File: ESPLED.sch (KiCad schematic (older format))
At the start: 44 parts, among them CON1 BARREL_JACK, J1 USB_B_Micro, J2 LED_CON_RGB, J3 LED_CON_WW, J4 MIC, P1 LED_CON_SCREW, P2 LED_CON_SCREW, P3 LED_CON_SCREW, Q1 IRLZ34N, Q2 IRLZ34N, Q3 IRLZ34N, Q4 IRLZ34N, Q5 IRLZ34N, SW1 Reset, SW2 Program, SW3 Mode, U1 AMS1117-3.3, U2 ESP-07v2, U3 INTERFACE-CH340G, U4 DS18B20, Y1 Crystal

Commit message: Ongoin reordering. Will probably
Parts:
- renumbered Q3 to Q1, Q1 to Q3
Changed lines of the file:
@@
 $EndComp
 $Comp
-L Transistor_FET:IRLZ34N Q3
+L Transistor_FET:IRLZ34N Q1
 U 1 1 5967CE85
 P 3200 3450
-F 0 "Q3" H 3400 3500 50  0000 L CNN
+F 0 "Q1" H 3400 3500 50  0000 L CNN
 F 1 "IRLZ34N" H 3400 3400 50  0000 L CNN
 F 2 "Package_TO_SOT_THT:TO-220-3_Horizontal_TabDown" H 3400 3550 50  0001 C CNN
@@
 $EndComp
 $Comp
-L Transistor_FET:IRLZ34N Q1
+L Transistor_FET:IRLZ34N Q3
 U 1 1 5967CF69
 P 1350 3450
-F 0 "Q1" H 1550 3500 50  0000 L CNN
+F 0 "Q3" H 1550 3500 50  0000 L CNN
 F 1 "IRLZ34N" H 1550 3400 50  0000 L CNN
 F 2 "Package_TO_SOT_THT:TO-220-3_Horizontal_TabDown" H 1550 3550 50  0001 C CNN

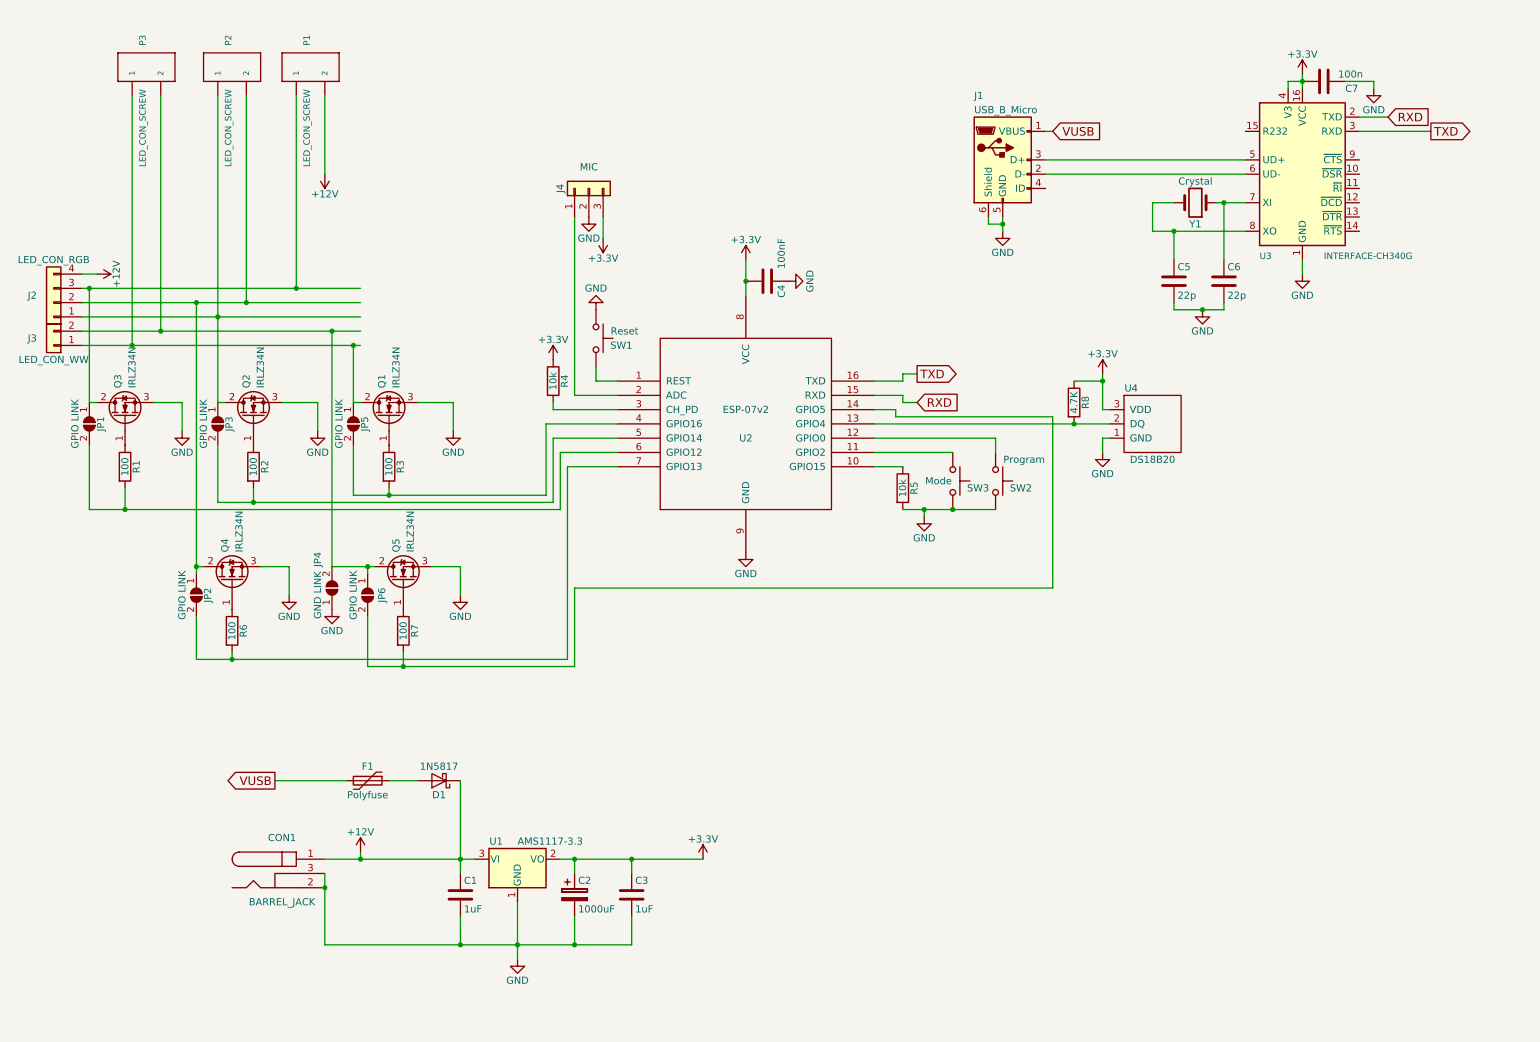
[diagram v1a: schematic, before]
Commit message: Routing done! Next step: verification
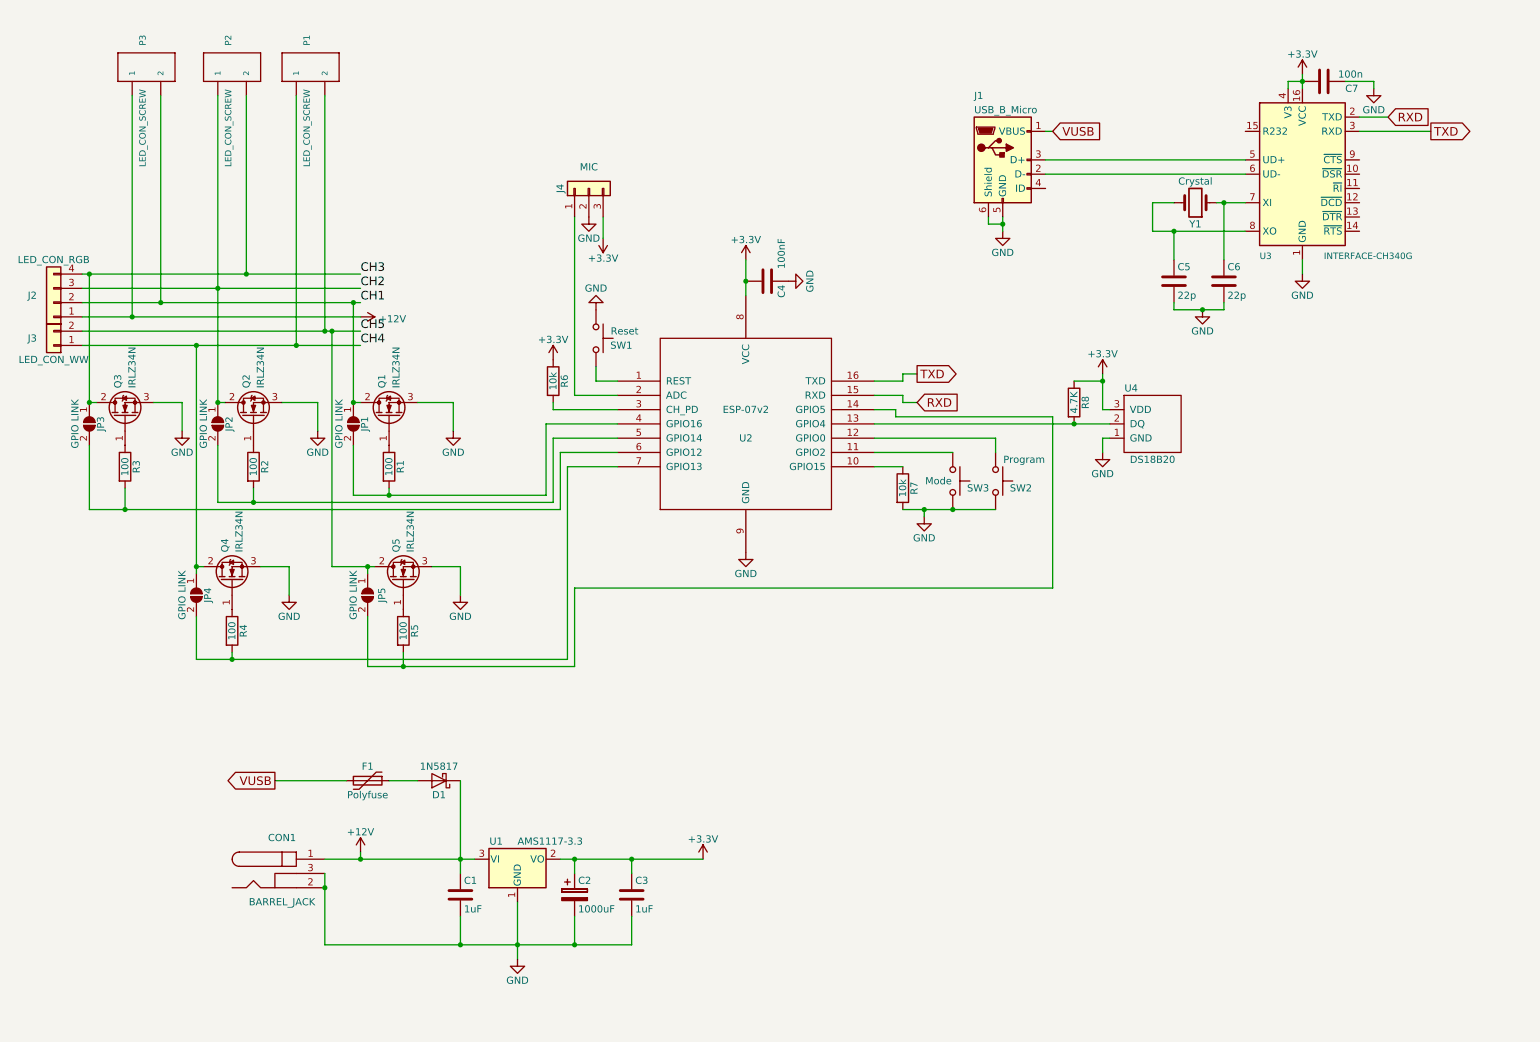
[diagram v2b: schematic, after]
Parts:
- removed JP4: GND LINK, Jumper:SolderJumper-2_P1.3mm_Open_TrianglePad1.0x1.5mm, symbol Jumper:SolderJumper_2_Open
- renumbered JP5 to JP1, JP3 to JP2, JP1 to JP3, JP2 to JP4, JP6 to JP5, R3 to R1, R1 to R3, R6 to R4, R7 to R5, R4 to R6, R5 to R7
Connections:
- net labels added: CH1, CH2, CH3, CH4, CH5
- wire segments 161 -> 162
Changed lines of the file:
@@
 $EndComp
 $Comp
-L power:+12V #PWR08
-U 1 1 5967D3E3
-P 1150 2450
-F 0 "#PWR08" H 1150 2300 50  0001 C CNN
-F 1 "+12V" H 1150 2590 50  0000 C CNN
-F 2 "" H 1150 2450 50  0000 C CNN
-F 3 "" H 1150 2450 50  0000 C CNN
-	1    1150 2450
-	0    1    1    0
-$EndComp
-$Comp
-L Device:R R3
+L Device:R R1
 U 1 1 5967D7DD
 P 3200 3800
-F 0 "R3" V 3280 3800 50  0000 C CNN
+F 0 "R1" V 3280 3800 50  0000 C CNN
 F 1 "100" V 3200 3800 50  0000 C CNN
 F 2 "Resistor_SMD:R_0603_1608Metric_Pad1.05x0.95mm_HandSolder" V 3130 3800 50  0001 C CNN
@@
 $EndComp
 $Comp
-L Device:R R1
+L Device:R R3
 U 1 1 5967D86A
 P 1350 3800
-F 0 "R1" V 1430 3800 50  0000 C CNN
+F 0 "R3" V 1430 3800 50  0000 C CNN
 F 1 "100" V 1350 3800 50  0000 C CNN
 F 2 "Resistor_SMD:R_0603_1608Metric_Pad1.05x0.95mm_HandSolder" V 1280 3800 50  0001 C CNN
@@
 $EndComp
 $Comp
-L Device:R R4
+L Device:R R6
 U 1 1 5967E72B
 P 4350 3200
-F 0 "R4" V 4430 3200 50  0000 C CNN
+F 0 "R6" V 4430 3200 50  0000 C CNN
 F 1 "10k" V 4350 3200 50  0000 C CNN
 F 2 "Resistor_SMD:R_0603_1608Metric_Pad1.05x0.95mm_HandSolder" V 4280 3200 50  0001 C CNN
@@
 $EndComp
 $Comp
-L Device:R R5
+L Device:R R7
 U 1 1 5967E7A8
 P 6800 3950
-F 0 "R5" V 6880 3950 50  0000 C CNN
+F 0 "R7" V 6880 3950 50  0000 C CNN
 F 1 "10k" V 6800 3950 50  0000 C CNN
 F 2 "Resistor_SMD:R_0603_1608Metric_Pad1.05x0.95mm_HandSolder" V 6730 3950 50  0001 C CNN
@@
 $EndComp
 $Comp
-L power:+12V #PWR015
-U 1 1 5A9872D9
-P 2750 1750
-F 0 "#PWR015" H 2750 1600 50  0001 C CNN
-F 1 "+12V" H 2750 1890 50  0000 C CNN
-F 2 "" H 2750 1750 50  0001 C CNN
-F 3 "" H 2750 1750 50  0001 C CNN
-	1    2750 1750
-	-1   0    0    1
-$EndComp
-$Comp
 L Switch:SW_Push SW3
 U 1 1 5BF9C7E1
@@
 $EndComp
 $Comp
-L Device:R R6
+L Device:R R4
 U 1 1 5BFC8C99
 P 2100 4950
-F 0 "R6" V 2180 4950 50  0000 C CNN
+F 0 "R4" V 2180 4950 50  0000 C CNN
 F 1 "100" V 2100 4950 50  0000 C CNN
 F 2 "Resistor_SMD:R_0603_1608Metric_Pad1.05x0.95mm_HandSolder" V 2030 4950 50  0001 C CNN
@@
 $EndComp
 $Comp
-L Device:R R7
+L Device:R R5
 U 1 1 5BFC8EE1
 P 3300 4950
-F 0 "R7" V 3380 4950 50  0000 C CNN
+F 0 "R5" V 3380 4950 50  0000 C CNN
 F 1 "100" V 3300 4950 50  0000 C CNN
 F 2 "Resistor_SMD:R_0603_1608Metric_Pad1.05x0.95mm_HandSolder" V 3230 4950 50  0001 C CNN
@@
 $EndComp
 $Comp
-L Jumper:SolderJumper_2_Open JP5
+L Jumper:SolderJumper_2_Open JP1
 U 1 1 5BFD5B1D
 P 2950 3500
-F 0 "JP5" H 2950 3580 50  0000 C CNN
+F 0 "JP1" H 2950 3580 50  0000 C CNN
 F 1 "GPIO LINK" H 2950 3400 50  0000 C CNN
 F 2 "Jumper:SolderJumper-2_P1.3mm_Open_RoundedPad1.0x1.5mm" H 2950 3500 50  0001 C CNN
@@
 $EndComp
 $Comp
-L Jumper:SolderJumper_2_Open JP3
+L Jumper:SolderJumper_2_Open JP2
 U 1 1 5BFD5BE2
 P 2000 3500
-F 0 "JP3" H 2000 3580 50  0000 C CNN
+F 0 "JP2" H 2000 3580 50  0000 C CNN
 F 1 "GPIO LINK" H 2000 3400 50  0000 C CNN
 F 2 "Jumper:SolderJumper-2_P1.3mm_Open_RoundedPad1.0x1.5mm" H 2000 3500 50  0001 C CNN
@@
 $EndComp
 $Comp
-L Jumper:SolderJumper_2_Open JP1
+L Jumper:SolderJumper_2_Open JP3
 U 1 1 5BFD5C80
 P 1100 3500
-F 0 "JP1" H 1100 3580 50  0000 C CNN
+F 0 "JP3" H 1100 3580 50  0000 C CNN
 F 1 "GPIO LINK" H 1100 3400 50  0000 C CNN
 F 2 "Jumper:SolderJumper-2_P1.3mm_Open_RoundedPad1.0x1.5mm" H 1100 3500 50  0001 C CNN
@@
 $EndComp
 $Comp
-L Jumper:SolderJumper_2_Open JP2
+L Jumper:SolderJumper_2_Open JP4
 U 1 1 5BFD609D
 P 1850 4700
-F 0 "JP2" H 1850 4780 50  0000 C CNN
+F 0 "JP4" H 1850 4780 50  0000 C CNN
 F 1 "GPIO LINK" H 1850 4600 50  0000 C CNN
 F 2 "Jumper:SolderJumper-2_P1.3mm_Open_RoundedPad1.0x1.5mm" H 1850 4700 50  0001 C CNN
@@
 $EndComp
 $Comp
-L Jumper:SolderJumper_2_Open JP6
+L Jumper:SolderJumper_2_Open JP5
 U 1 1 5BFD707F
 P 3050 4700
-F 0 "JP6" H 3050 4800 50  0000 C CNN
+F 0 "JP5" H 3050 4800 50  0000 C CNN
 F 1 "GPIO LINK" H 3050 4600 50  0000 C CNN
 F 2 "Jumper:SolderJumper-2_P1.3mm_Open_RoundedPad1.0x1.5mm" H 3050 4700 50  0001 C CNN
@@
 	1    3050 4700
 	0    1    1    0
-$EndComp
-$Comp
-L Jumper:SolderJumper_2_Open JP4
-U 1 1 5BFD7EB1
-P 2800 4650
-F 0 "JP4" H 3000 4750 50  0000 C CNN
-F 1 "GND LINK" H 2750 4750 50  0000 C CNN
-F 2 "Jumper:SolderJumper-2_P1.3mm_Open_TrianglePad1.0x1.5mm" H 2800 4650 50  0001 C CNN
-F 3 "" H 2800 4650 50  0001 C CNN
-	1    2800 4650
-	0    -1   -1   0
-$EndComp
-$Comp
-L power:GND #PWR023
-U 1 1 5BFDBFB3
-P 2800 4800
-F 0 "#PWR023" H 2800 4550 50  0001 C CNN
-F 1 "GND" H 2800 4650 50  0000 C CNN
-F 2 "" H 2800 4800 50  0001 C CNN
-F 3 "" H 2800 4800 50  0001 C CNN
-	1    2800 4800
-	1    0    0    -1
 $EndComp
 $Comp
@@
 	3650 3350 3650 3550
 Wire Wire Line
-	1050 2650 1850 2650
-Wire Wire Line
-	1150 2450 1050 2450
-Wire Wire Line
 	3200 4000 3200 3950
 Wire Wire Line
@@
 	4650 3200 4800 3200
 Wire Wire Line
-	2750 1200 2750 1750
-Wire Wire Line
 	4900 7150 4900 6950
 Connection ~ 5700 2500
@@
 	2950 4000 3200 4000
 Wire Wire Line
-	3000 2550 2550 2550
-Wire Wire Line
-	1050 2750 2000 2750
-Wire Wire Line
-	1050 2850 1600 2850
-Wire Wire Line
-	1050 2950 1400 2950
-Wire Wire Line
 	6750 3450 7850 3450
 Wire Wire Line
@@
 	1900 4500 1850 4500
 Wire Wire Line
-	1850 2650 1850 4500
-Wire Wire Line
 	1100 3350 1150 3350
 Wire Wire Line
@@
 Wire Wire Line
 	2000 3350 2050 3350
-Wire Wire Line
-	1100 3350 1100 2550
-Connection ~ 1100 2550
-Connection ~ 1850 2650
-Connection ~ 1850 4500
-Wire Wire Line
-	2000 1200 2000 2750
-Connection ~ 2000 2750
-Wire Wire Line
-	2800 4500 2800 2850
-Connection ~ 2800 2850
-Wire Wire Line
-	2950 3350 2950 2950
-Connection ~ 2950 2950
-Wire Wire Line
-	2550 1200 2550 2550
-Connection ~ 2550 2550
-Wire Wire Line
-	2200 1200 2200 2650
-Connection ~ 2200 2650
-Wire Wire Line
-	1600 1200 1600 2850
-Connection ~ 1600 2850
-Wire Wire Line
-	1400 1200 1400 2950
-Connection ~ 1400 2950
 Wire Wire Line
 	3500 4500 3700 4500
@@
 	3200 4000 4300 4000
 Wire Wire Line
-	1100 2550 1050 2550
-Wire Wire Line
-	1850 2650 2200 2650
-Wire Wire Line
 	1850 4500 1850 4550
-Wire Wire Line
-	2000 2750 3000 2750
-Wire Wire Line
-	2000 2750 2000 3350
-Wire Wire Line
-	2800 2850 3000 2850
-Wire Wire Line
-	2950 2950 3000 2950
-Wire Wire Line
-	2550 2550 1100 2550
-Wire Wire Line
-	2200 2650 3000 2650
-Wire Wire Line
-	1600 2850 2800 2850
-Wire Wire Line
-	1400 2950 2950 2950
 Wire Wire Line
 	8000 3500 8250 3500
@@
 	-1   0    0    1
 $EndComp
+Wire Wire Line
+	1050 2450 1100 2450
+$Comp
+L power:+12V #PWR0101
+U 1 1 5C362ECD
+P 3000 2750
+F 0 "#PWR0101" H 3000 2600 50  0001 C CNN
+F 1 "+12V" V 3015 2878 50  0000 L CNN
+F 2 "" H 3000 2750 50  0001 C CNN
+F 3 "" H 3000 2750 50  0001 C CNN
+	1    3000 2750
+	0    1    1    0
+$EndComp
+Wire Wire Line
+	1050 2750 1400 2750
+Wire Wire Line
+	1050 2550 2000 2550
+Wire Wire Line
+	1050 2650 1600 2650
+Wire Wire Line
+	1050 2850 2750 2850
+Wire Wire Line
+	1050 2950 1850 2950
+Wire Wire Line
+	2950 3350 2950 2650
+Connection ~ 2950 3350
+Connection ~ 2950 2650
+Wire Wire Line
+	2950 2650 3000 2650
+Wire Wire Line
+	1400 1200 1400 2750
+Connection ~ 1400 2750
+Wire Wire Line
+	1400 2750 3000 2750
+Wire Wire Line
+	1600 1200 1600 2650
+Connection ~ 1600 2650
+Wire Wire Line
+	1600 2650 2950 2650
+Wire Wire Line
+	2000 1200 2000 2550
+Connection ~ 2000 2550
+Wire Wire Line
+	2000 2550 3000 2550
+Wire Wire Line
+	2200 1200 2200 2450
+Connection ~ 2200 2450
+Wire Wire Line
+	2200 2450 3000 2450
+Wire Wire Line
+	2550 1200 2550 2950
+Connection ~ 2550 2950
+Wire Wire Line
+	2550 2950 3000 2950
+Wire Wire Line
+	2750 1200 2750 2850
+Connection ~ 2750 2850
+Wire Wire Line
+	2750 2850 2800 2850
+Wire Wire Line
+	2000 3350 2000 2550
+Connection ~ 2000 3350
+Wire Wire Line
+	1100 3350 1100 2450
+Connection ~ 1100 3350
+Connection ~ 1100 2450
+Wire Wire Line
+	1100 2450 2200 2450
+Wire Wire Line
+	1850 4500 1850 2950
+Connection ~ 1850 4500
+Connection ~ 1850 2950
+Wire Wire Line
+	1850 2950 2550 2950
+Wire Wire Line
+	2800 4500 2800 2850
+Connection ~ 2800 2850
+Wire Wire Line
+	2800 2850 3000 2850
+Text Label 3000 2650 0    60   ~ 0
+CH1
+Text Label 3000 2550 0    60   ~ 0
+CH2
+Text Label 3000 2450 0    60   ~ 0
+CH3
+Text Label 3000 2950 0    60   ~ 0
+CH4
+Text Label 3000 2850 0    60   ~ 0
+CH5
 $EndSCHEMATC

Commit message: layout finished. Adding logic level converter
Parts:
- U3: footprint Package_SO:SOIC-16W_5.3x10.2mm_P1.27mm -> Package_SO:SOP-16_4.4x10.4mm_P1.27mm
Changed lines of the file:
@@
 F 0 "U3" H 9300 1150 45  0000 L BNN
 F 1 "INTERFACE-CH340G" H 9750 1150 45  0000 L BNN
-F 2 "Package_SO:SOIC-16W_5.3x10.2mm_P1.27mm" H 9600 1750 60  0001 C CNN
+F 2 "Package_SO:SOP-16_4.4x10.4mm_P1.27mm" H 9600 1750 60  0001 C CNN
 F 3 "" H 9600 1750 60  0001 C CNN
 F 4 "CH340T" H 9630 1900 20  0001 C CNN "MPN"
